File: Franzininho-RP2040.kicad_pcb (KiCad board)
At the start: 2 copper layers, 37 parts, among them J1 USB_B_Micro, J2 Conn_01x02, J3 Conn_01x04, J4 Conn_01x17, J5 Conn_01x17, SW1 SW_Push, U1 RP2040, U2 NCP1117-3.3_SOT223, U3 W25Q128JVS, Y1 12MHz

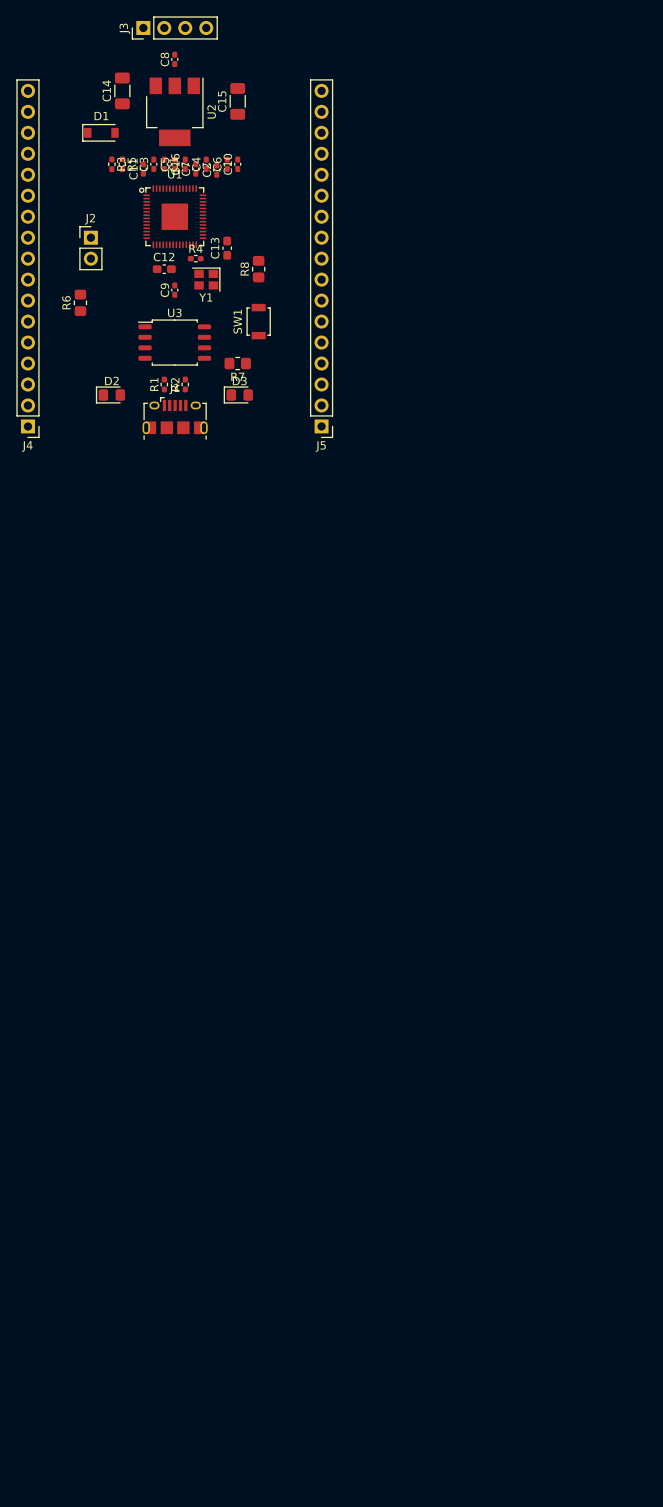
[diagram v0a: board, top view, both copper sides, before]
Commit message: Adição de modelos 3D e melhorias
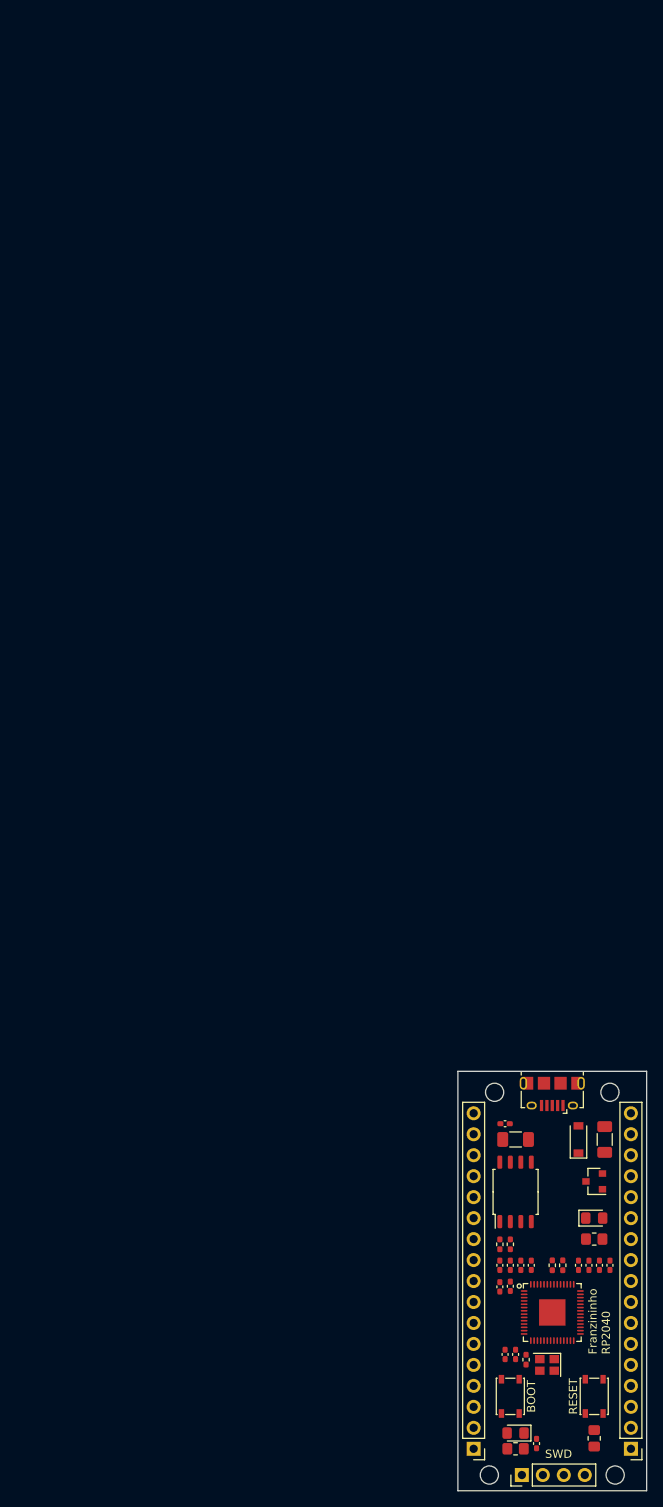
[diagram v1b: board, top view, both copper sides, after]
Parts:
- removed J2: Conn_01x02, Connector_PinHeader_2.54mm:PinHeader_1x02_P2.54mm_Vertical
- removed SW1: SW_Push, Button_Switch_SMD:SW_SPST_B3U-1000P
- added BOOT: SW_Push, Button_Switch_SMD:SW_SPST_PTS810, F.Cu at (144.8, 111.1)
- added H1: MountingHole, MountingHole:MountingHole_2.2mm_M2, F.Cu at (142.9, 74.3)
- added H2: MountingHole, MountingHole:MountingHole_2.2mm_M2, F.Cu at (156.8, 74.3)
- added H3: MountingHole, MountingHole:MountingHole_2.2mm_M2, F.Cu at (142.2, 120.7)
- added H4: MountingHole, MountingHole:MountingHole_2.2mm_M2, F.Cu at (157.5, 120.7)
- added RESET: SW_Push, Button_Switch_SMD:SW_SPST_PTS810, F.Cu at (154.9, 111.1)
- C12, C13: footprint Capacitor_SMD:C_0603_1608Metric_Pad1.08x0.95mm_HandSolder -> Capacitor_SMD:C_0402_1005Metric_Pad0.74x0.62mm_HandSolder
- U2: value NCP1117-3.3_SOT223 -> XC6206P332MR; footprint Package_TO_SOT_SMD:SOT-223-3_TabPin2 -> Package_TO_SOT_SMD:SOT-23
- moved SWD 181.2 mm to (146.2, 120.7)
- moved R6 148.5 mm to (145.4, 117.5), turned to 0 degrees
- moved R8 147.3 mm to (154.9, 116.2), turned to 270 degrees
- moved C9 146.4 mm to (148.0, 116.8)
- moved C3 142.6 mm to (144.8, 97.8)
- moved C11 142.1 mm to (143.5, 97.9)
- moved C4 141.2 mm to (154.3, 95.2)
- moved C10 140.8 mm to (156.8, 95.2)
- moved C6 140.8 mm to (155.6, 95.2)
- moved U1 140.4 mm to (149.9, 101.0)
- moved C14 139.8 mm to (156.2, 80.0)
- moved C2 139.7 mm to (153.0, 95.2)
- moved C1 139.4 mm to (143.5, 95.2)
- moved C16 139.4 mm to (146.1, 95.2)
- moved C5 139.4 mm to (144.8, 95.2)
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- renumbered J3 to SWD, J1 to USB
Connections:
- net Net-(C13-Pad1) renamed /XOUT_R
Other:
- board outline added: 22.9 x 50.8 mm
- board text added: "0"
- board text added: "1"
- board text added: "10"
- board text added: "11"
- board text added: "12"
- board text added: "13"
- board text added: "14"
- board text added: "15"
- board text added: "16"
- board text added: "17"
- board text added: "18"
- board text added: "19"
- board text added: "2"
- board text added: "20"
- board text added: "21"
- board text added: "22"
- board text added: "23"
- board text added: "24"
- board text added: "25"
- board text added: "26"
- board text added: "27"
- board text added: "28"
- board text added: "3"
- board text added: "3V3"
- board text added: "4"
- board text added: "5"
- board text added: "5V"
- board text added: "6"
- board text added: "7"
- board text added: "8"
- board text added: "9"
- board text added: "Franzininho RP2040"
- board text added: "GND"
- board text added: "SWCLK"
- board text added: "SWDIO"

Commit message: Atualização para KiCad 6
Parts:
- C14, C15: footprint Capacitor_SMD:C_1206_3216Metric_Pad1.33x1.80mm_HandSolder -> Capacitor_SMD:C_0805_2012Metric_Pad1.18x1.45mm_HandSolder
- R6, R7, R8: footprint Resistor_SMD:R_0805_2012Metric_Pad1.20x1.40mm_HandSolder -> Resistor_SMD:R_0603_1608Metric_Pad0.98x0.95mm_HandSolder
- renumbered USB to J1, SWD to J3, BOOT to SW1, RESET to SW2
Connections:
- net /~RESET renamed /~{RESET}
- net /~USB_BOOT renamed /~{USB_BOOT}
- J1 pad 4: Net-(J1-Pad4) -> unconnected-(J1-Pad4)
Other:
- net class Default removed

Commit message: Atualização da PCB
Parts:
- added J2: Conn_01x07_Male, Connector_PinHeader_2.54mm:PinHeader_1x07_P2.54mm_Vertical, F.Cu at (214.1, 42.0)
- added J6: Micro_SD_Card, Connector_Card:microSD_HC_Wuerth_693072010801, F.Cu at (63.2, 98.5)
- added R10: 10k, Resistor_SMD:R_0603_1608Metric, F.Cu at (56.6, 108.8)
- added R11: DNF, Resistor_SMD:R_0603_1608Metric, F.Cu at (66.4, 85.5)
- added R9: 100k, Resistor_SMD:R_0603_1608Metric, F.Cu at (66.4, 88.0)
- added SW3: SW_Push, Button_Switch_THT:SW_PUSH-12mm, F.Cu at (196.1, 91.7)
- added SW4: SW_Push, Button_Switch_THT:SW_PUSH-12mm, F.Cu at (211.2, 71.3)
- added SW5: SW_Push, Button_Switch_THT:SW_PUSH-12mm, F.Cu at (219.2, 91.7)
- added SW6: SW_Push, Button_Switch_THT:SW_PUSH-12mm, F.Cu at (211.2, 94.4)
- added SW7: SW_Push, Button_Switch_THT:SW_PUSH-12mm, F.Cu at (142.8, 124.5)
- added SW8: SW_Push, Button_Switch_THT:SW_PUSH-12mm, F.Cu at (247.8, 74.6)
- added SW9: SW_Push, Button_Switch_THT:SW_PUSH-12mm, F.Cu at (244.8, 92.0)
- added U2: AP2112K-3.3, Package_TO_SOT_SMD:SOT-23-5, F.Cu at (61.8, 86.5)
- C1, C10, C11, C12, C13, C16, C2, C3, C4, C5, C6, C7, C8, C9: footprint Capacitor_SMD:C_0402_1005Metric_Pad0.74x0.62mm_HandSolder -> Capacitor_SMD:C_0603_1608Metric
- C14, C15: footprint Capacitor_SMD:C_0805_2012Metric_Pad1.18x1.45mm_HandSolder -> Capacitor_SMD:C_0603_1608Metric
- D1: value D_Schottky -> 1N5819W
- D2, D3: footprint LED_SMD:LED_0805_2012Metric_Pad1.15x1.40mm_HandSolder -> LED_SMD:LED_0603_1608Metric
- J1: footprint Connector_USB:USB_Micro-B_Amphenol_10118194_Horizontal -> Connector_USB:USB_Micro-B_Molex-105017-0001
- R1, R2, R3, R4, R5: footprint Resistor_SMD:R_0402_1005Metric_Pad0.72x0.64mm_HandSolder -> Resistor_SMD:R_0603_1608Metric
- R6, R7, R8: footprint Resistor_SMD:R_0603_1608Metric_Pad0.98x0.95mm_HandSolder -> Resistor_SMD:R_0603_1608Metric
- U1: footprint Biblioteca de footprints:QFN40P695X695X90-57T320N -> Biblioteca de footprints:RP2040-QFN-56
- Y1: footprint Crystal:Crystal_SMD_2520-4Pin_2.5x2.0mm -> Biblioteca de footprints:Crystal_SMD_HC49-US
- moved H1 89.3 mm to (75.9, 133.3)
- moved H2 89.3 mm to (89.9, 133.3)
- moved Y1 77.9 mm to (172.5, 33.0)
- moved R4 72.7 mm to (137.0, 34.7)
- moved C12 72.7 mm to (135.8, 34.0)
- moved C13 72.7 mm to (134.5, 34.0)
- moved C3 72.5 mm to (140.1, 25.4)
- moved C1 72.5 mm to (138.8, 22.9)
- moved C10 72.5 mm to (152.1, 22.9)
- moved C11 72.5 mm to (138.8, 25.5)
- moved C16 72.5 mm to (141.4, 22.9)
- moved C2 72.5 mm to (148.3, 22.9)
- moved C4 72.5 mm to (149.6, 22.9)
- moved C5 72.5 mm to (140.1, 22.9)
- moved C6 72.5 mm to (150.9, 22.9)
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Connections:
- U1 pad 12: /GPIO9 -> /BT_LEFT
- U1 pad 13: /GPIO10 -> /BT_RIGHT
- U1 pad 14: /GPIO11 -> /BT_UP
- U1 pad 15: /GPIO12 -> /BT_DOWN
- U1 pad 16: /GPIO13 -> /BT_A
- U1 pad 17: /GPIO14 -> /BT_B
- U1 pad 18: /GPIO15 -> /BT_MENU
- U1 pad 29: /GPIO18 -> /SD_CMD
- U1 pad 3: /GPIO1 -> /SD_CLK
- U1 pad 31: /GPIO20 -> /SD_DAT1
- U1 pad 32: /GPIO21 -> /SD_DAT2
- U1 pad 34: /GPIO22 -> /SD_DAT3
- U1 pad 4: /GPIO2 -> /DISPLAY_SCL
- U1 pad 5: /GPIO3 -> /DISPLAY_SDA
- U1 pad 6: /GPIO4 -> /DISPLAY_DC
- U1 pad 7: /GPIO5 -> /DISPLAY_RES
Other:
- board size 22.9 x 50.8 mm -> 88.4 x 100.1 mm
- board text removed: "Franzininho RP2040"

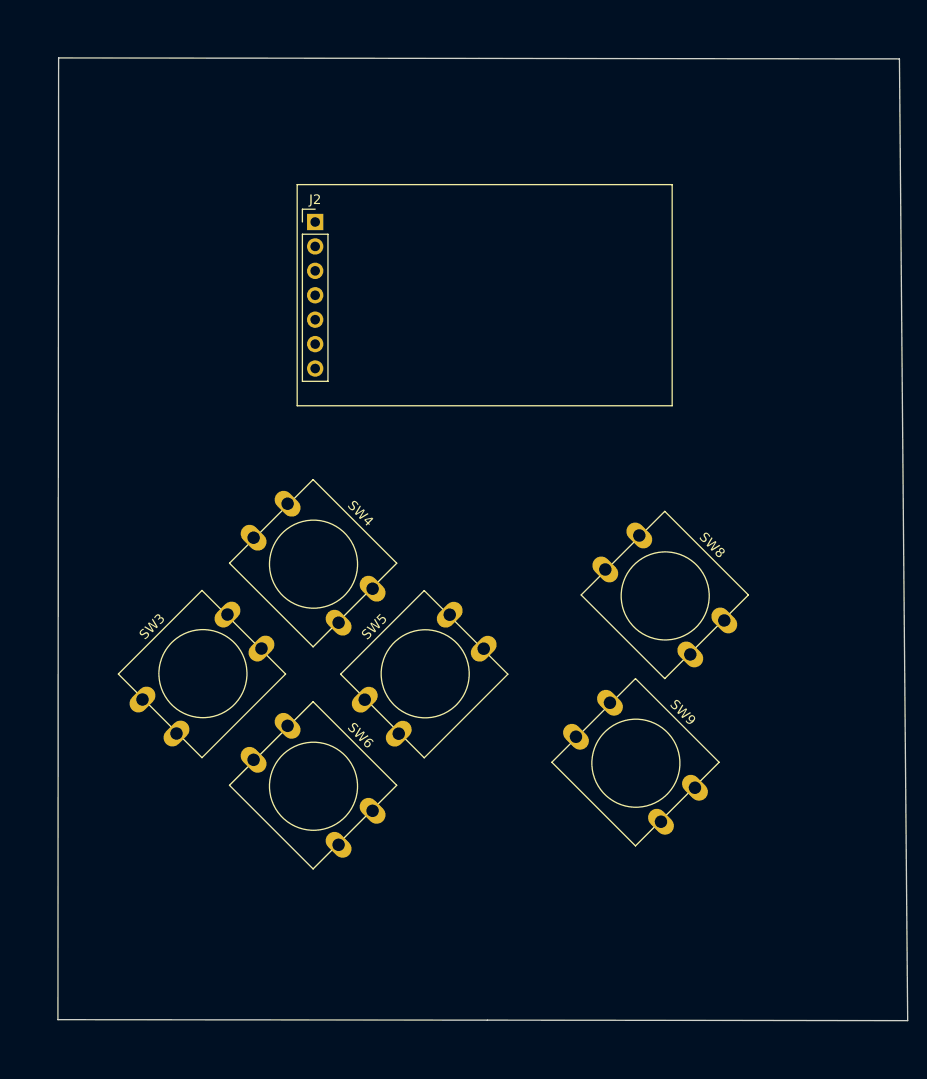
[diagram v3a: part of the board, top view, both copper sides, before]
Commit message: Ajuste do outline da placa
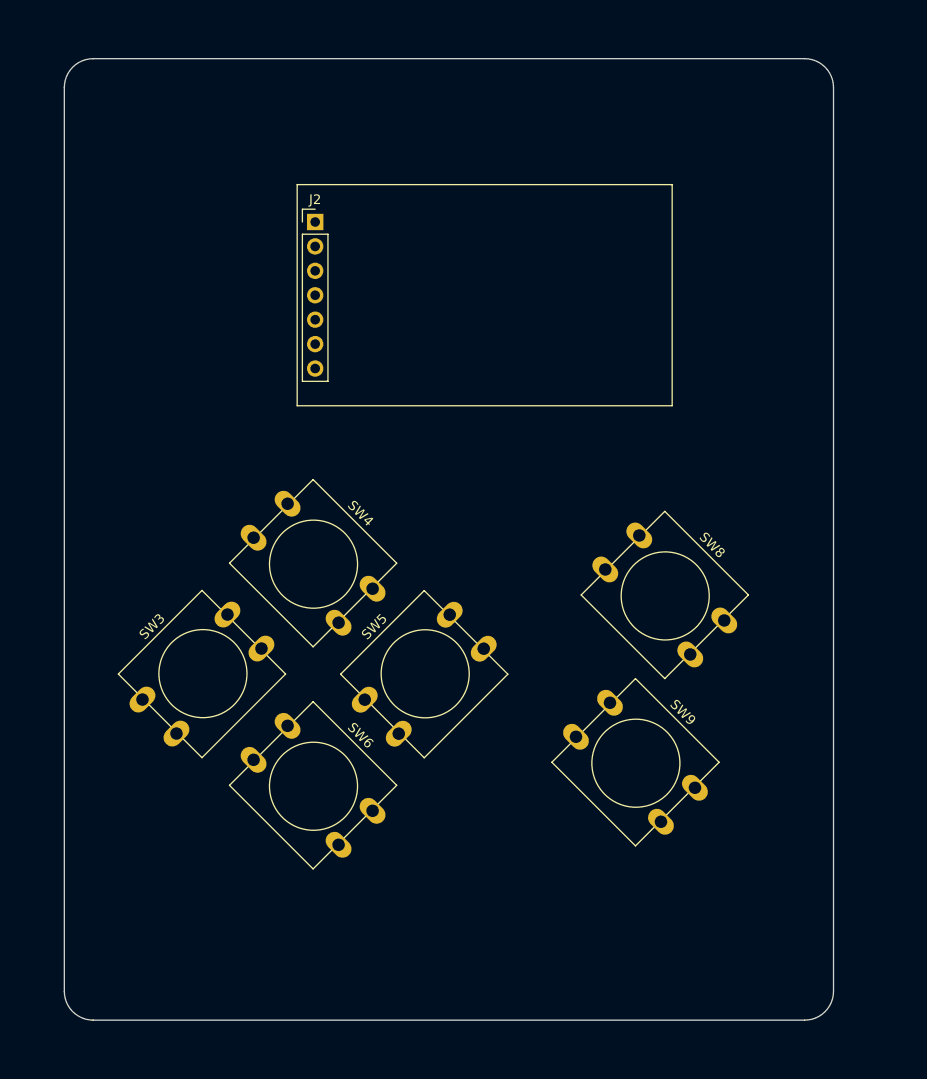
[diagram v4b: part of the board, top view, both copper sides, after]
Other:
- board size 88.4 x 100.1 mm -> 80 x 100 mm
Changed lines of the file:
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@@
   (gr_line (start 251.216998 38.1) (end 251.216998 61.100005) (layer "F.SilkS") (width 0.12))
   (gr_line (start 213.866 89.011) (end 234.129485 89.019941) (layer "Dwgs.User") (width 0.12))
+  (gr_line (start 270 75) (end 186 75) (layer "Dwgs.User") (width 0.1))
   (gr_line (start 213.875068 68.779646) (end 213.866 89.011) (layer "Dwgs.User") (width 0.12))
   (gr_line (start 193.602515 89.002059) (end 213.866 89.011) (layer "Dwgs.User") (width 0.12))
   (gr_line (start 213.866 89.011) (end 213.856932 109.242354) (layer "Dwgs.User") (width 0.12))
-  (gr_line (start 231.716999 38.1) (end 231.775 119.253) (layer "Dwgs.User") (width 0.1))
-  (gr_line (start 187.4045 24.9238) (end 187.3341 124.9492) (layer "Edge.Cuts") (width 0.05))
-  (gr_line (start 231.1179 24.9746) (end 187.4045 24.9238) (layer "Edge.Cuts") (width 0.05))
-  (gr_line (start 274.8567 25.0254) (end 231.1433 24.9746) (layer "Edge.Cuts") (width 0.05))
-  (gr_line (start 275.7134 125.0508) (end 232 125) (layer "Edge.Cuts") (width 0.05))
-  (gr_line (start 274.8567 25.0254) (end 275.7134 125.0508) (layer "Edge.Cuts") (width 0.05))
-  (gr_line (start 232 125) (end 187.3341 124.9492) (layer "Edge.Cuts") (width 0.05))
+  (gr_line (start 228 130) (end 228 20) (layer "Dwgs.User") (width 0.1))
+  (gr_line (start 265 125) (end 191 125) (layer "Edge.Cuts") (width 0.05))
+  (gr_arc (start 268 122) (mid 267.12132 124.12132) (end 265 125) (layer "Edge.Cuts") (width 0.1))
+  (gr_line (start 191 25) (end 265 25) (layer "Edge.Cuts") (width 0.05))
+  (gr_line (start 188 122) (end 188 28) (layer "Edge.Cuts") (width 0.05))
+  (gr_line (start 268 28) (end 268 122) (layer "Edge.Cuts") (width 0.05))
+  (gr_arc (start 188 28) (mid 188.87868 25.87868) (end 191 25) (layer "Edge.Cuts") (width 0.1))
+  (gr_arc (start 191 125) (mid 188.87868 124.12132) (end 188 122) (layer "Edge.Cuts") (width 0.1))
+  (gr_arc (start 265 25) (mid 267.12132 25.87868) (end 268 28) (layer "Edge.Cuts") (width 0.1))
   (gr_text "GND" (at 156.845 114.935) (layer "B.SilkS")
     (effects (font (size 1 1) (thickness 0.15)) (justify mirror))
@@
     (effects (font (size 1 1) (thickness 0.15)) (justify mirror))
   )
+  (dimension (type aligned) (layer "Dwgs.User")
+    (pts (xy 188 124.9492) (xy 268 124.9492))
+    (height 15.0508)
+    (gr_text "80.0000 mm" (at 228 138.85) (layer "Dwgs.User")
+      (effects (font (size 1 1) (thickness 0.15)))
+    )
+    (format (units 3) (units_format 1) (precision 4))
+    (style (thickness 0.1) (arrow_length 1.27) (text_position_mode 0) (extension_height 0.58642) (extension_offset 0.5) keep_text_aligned)
+  )
+  (dimension (type aligned) (layer "Dwgs.User")
+    (pts (xy 268 25) (xy 268 125))
+    (height -12)
+    (gr_text "100.0000 mm" (at 278.85 75 90) (layer "Dwgs.User")
+      (effects (font (size 1 1) (thickness 0.15)))
+    )
+    (format (units 3) (units_format 1) (precision 4))
+    (style (thickness 0.1) (arrow_length 1.27) (text_position_mode 0) (extension_height 0.58642) (extension_offset 0.5) keep_text_aligned)
+  )
   (group "" (id a4646a71-a41a-457e-b69f-0409bde12e01)
